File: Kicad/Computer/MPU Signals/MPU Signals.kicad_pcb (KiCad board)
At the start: 2 copper layers, 128.3 x 61 mm, 79 parts, among them IC1 FAN2558S38X, IC10 74LVC1G17GV,125, IC11 ATF22V10C-10SU, IC12 ATF22V10C-10SU, IC13 ATF22V10C-10SU, IC14 ATF22V10C-10SU, IC2 W65C816S6TQG-14, IC3 74LVC573AD,112, IC4 74LVC4245APW,118, IC5 74LVC04AD,118, IC6 74LVC32APW,118, IC7 74LVC1G08GV,125, IC8 74LVC11PW,112, IC9 NE555DRG4, J1 Conn_01x02_Male, J10 Conn_01x02_Male, J11 Conn_01x10_Male, J12 Conn_01x16_Male, J13 Conn_01x08_Male, J14 Conn_01x12_Male, J15 Conn_01x16_Male, J16 Conn_01x12_Male, J17 Conn_02x05_Counter_Clockwise, J18 Conn_02x05_Counter_Clockwise, J19 SamacSys_Parts:Pin_Header_1.2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, J2 Conn_01x02_Male, J20 Conn_02x05_Counter_Clockwise, J21 SamacSys_Parts:Pin_Header_1.2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, J22 Conn_02x05_Counter_Clockwise, J23 SamacSys_Parts:Pin_Header_1.2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, J24 Conn_02x05_Counter_Clockwise, J3 Conn_01x02_Male, J4 Conn_01x10_Male, J5 Conn_01x02_Male, J6 Conn_01x02_Male, J7 Conn_01x16_Male, J8 Conn_01x02_Male, J9 Conn_01x02_Male

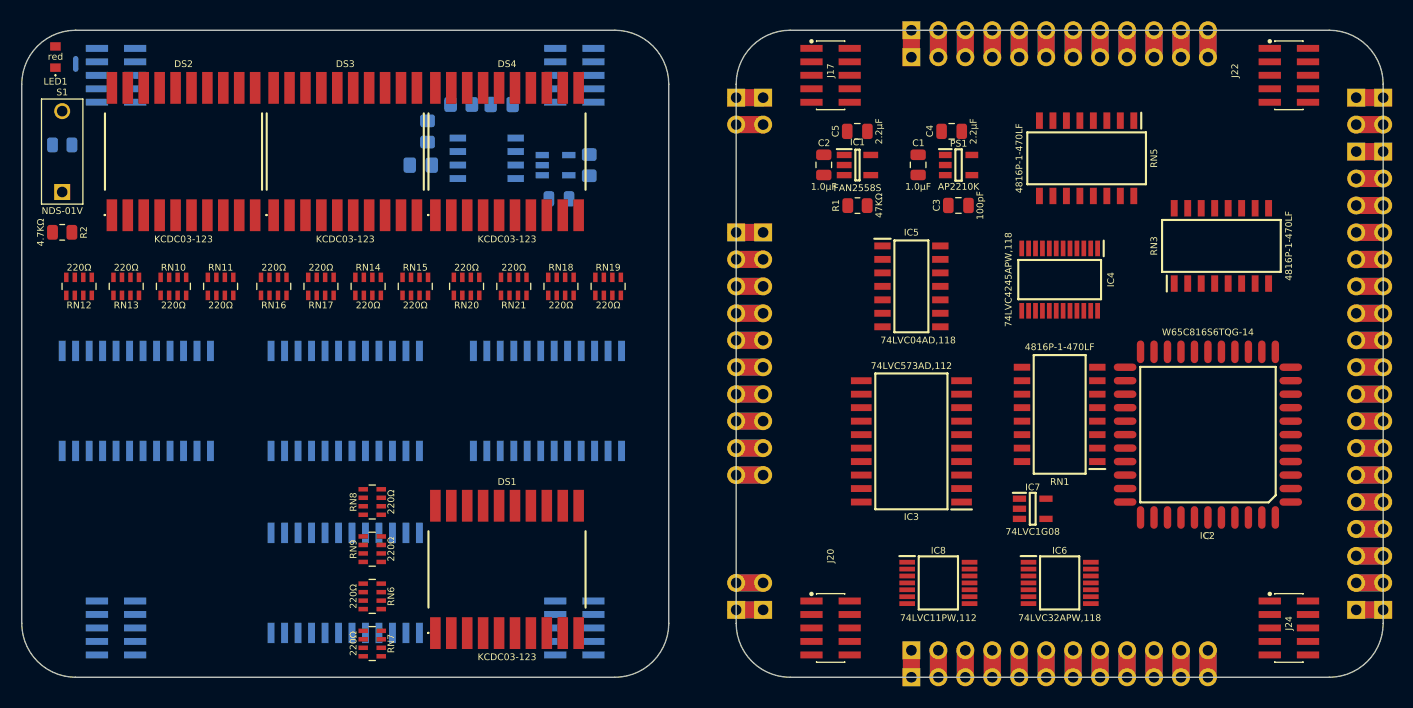
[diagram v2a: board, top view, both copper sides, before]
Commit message: Added a correct W65C816S footprint.
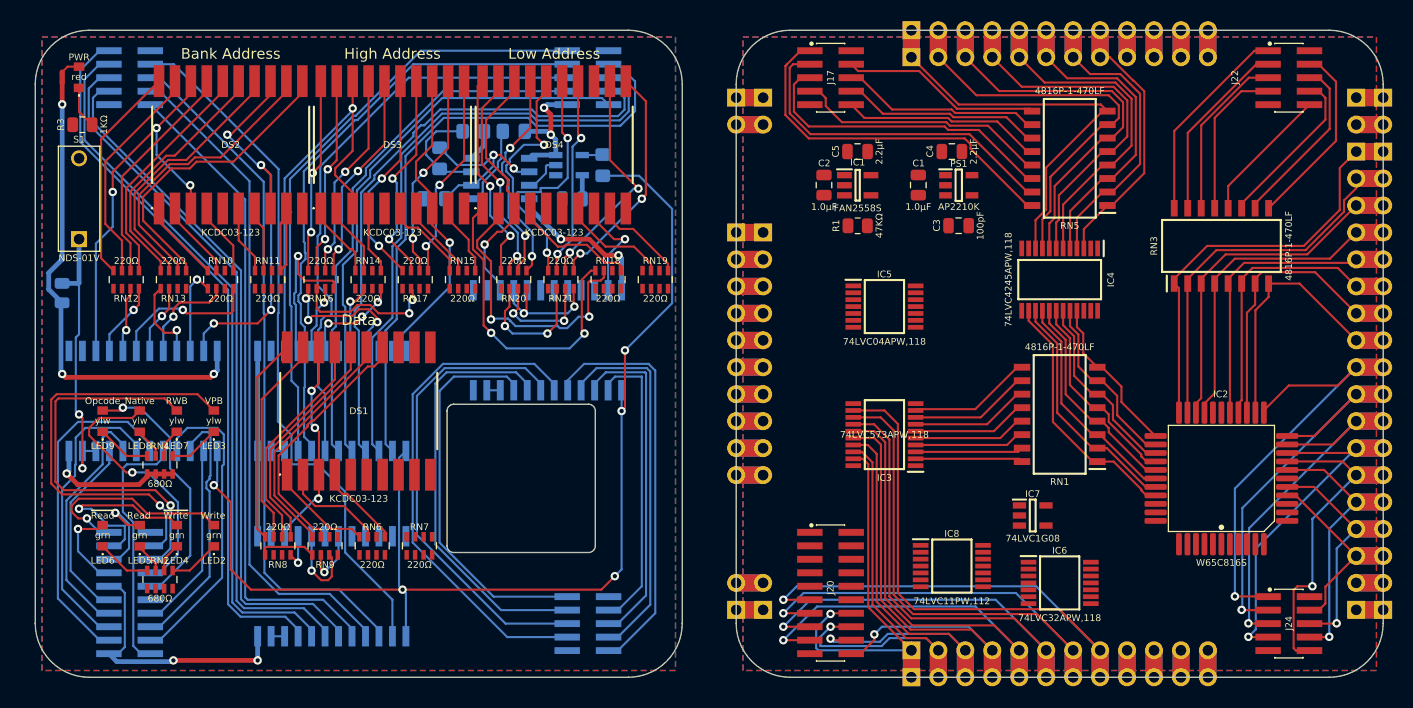
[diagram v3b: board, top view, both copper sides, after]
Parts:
- added LED2: 150224VS73100A, SamacSys_Parts:150224VS73100A, F.Cu at (77.8, 122.6)
- added LED3: 150224YS73100A, SamacSys_Parts:150224BS73100A, F.Cu at (77.8, 111.8)
- added LED4: 150224VS73100A, SamacSys_Parts:150224VS73100A, F.Cu at (74.3, 122.6)
- added LED5: 150224VS73100A, SamacSys_Parts:150224VS73100A, F.Cu at (70.8, 122.6)
- added LED6: 150224VS73100A, SamacSys_Parts:150224VS73100A, F.Cu at (67.3, 122.6)
- added LED7: 150224YS73100A, SamacSys_Parts:150224BS73100A, F.Cu at (74.3, 111.8)
- added LED8: 150224YS73100A, SamacSys_Parts:150224BS73100A, F.Cu at (70.8, 111.8)
- added LED9: 150224YS73100A, SamacSys_Parts:150224BS73100A, F.Cu at (67.3, 111.8)
- added RN2: CAY16-681J4LF, SamacSys_Parts:CAY16-J4, F.Cu at (72.7, 126.7)
- added RN4: CAY16-681J4LF, SamacSys_Parts:CAY16-J4, F.Cu at (72.7, 115.9)
- IC2: value W65C816S6TQG-14 -> W65C816S; footprint SamacSys_Parts:PLCC127P1752X1752X457-44N -> SamacSys_Parts:W65C816 PLCC 0.8mm 44 Pin
- IC3: value 74LVC573AD,112 -> 74LVC573APW,118; footprint SamacSys_Parts:SOIC127P1032X265-20N -> SamacSys_Parts:SOP65P640X110-20N
- IC5: value 74LVC04AD,118 -> 74LVC04APW,118; footprint SamacSys_Parts:SOIC127P600X175-14N -> SamacSys_Parts:SOP65P640X110-14N
- J19: footprint SamacSys_Parts:Pin_Header_1.27mm 2x05 -> SamacSys_Parts:Pin_Header_1.27mm 2x10
- J20: footprint SamacSys_Parts:Pin_Socket_1.27mm 2x05 -> SamacSys_Parts:Pin_Socket_1.27mm 2x10
- NT1, R3: moved to F.Cu
- R2: moved to B.Cu
- moved DS1 20.4 mm to (91.4, 110.8)
- moved RN7 10.2 mm to (97.2, 123.5), turned to 0 degrees
- moved RN8 9.80 mm to (83.8, 123.5), turned to 180 degrees
- moved RN17 8.91 mm to (96.8, 98.4)
- moved R2 5.72 mm to (63.5, 99.7), turned to 0 degrees
- moved IC14 5.72 mm to (109.2, 104.1)
- moved RN6 4.76 mm to (92.7, 123.5), turned to 0 degrees
- moved S1 4.72 mm to (65.1, 94.6)
- moved RN11 4.49 mm to (82.9, 98.4)
- moved RN13 4.49 mm to (74.0, 98.4)
- moved RN15 4.49 mm to (101.2, 98.4)
- moved DS2 4.49 mm to (79.4, 85.7)
- moved DS3 4.49 mm to (94.6, 85.7)
- moved DS4 4.49 mm to (109.9, 85.7)
- moved RN10 4.49 mm to (78.4, 98.4)
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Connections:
- IC4 pad 1: unconnected-(IC4-Pad1) -> /5V
- IC5 pad 11: unconnected-(IC5-Pad11) -> GND
- IC5 pad 13: unconnected-(IC5-Pad13) -> GND
- IC5 pad 9: unconnected-(IC5-Pad9) -> GND
- J15 pad 1: /BA7 -> /BA0
- J15 pad 2: /BA6 -> /BA1
- J15 pad 3: /BA5 -> /BA2
- J15 pad 4: /BA4 -> /BA3
- J15 pad 5: /BA3 -> /BA4
- J15 pad 6: /BA2 -> /BA5
- J15 pad 7: /BA1 -> /BA6
- J15 pad 8: /BA0 -> /BA7
- J16 pad 1: /BA7 -> /BA0
- J16 pad 2: /BA6 -> /BA1
- J16 pad 3: /BA5 -> /BA2
- J16 pad 4: /BA4 -> /BA3
- J16 pad 5: /BA3 -> /BA4
- J16 pad 6: /BA2 -> /BA5
- J16 pad 7: /BA1 -> /BA6
- J16 pad 8: /BA0 -> /BA7
- J19 pad 1: /5V_{TOP} -> /3.8V_{TOP}
- J19 pad 10: /BA7_{TOP} -> /BA3_{TOP}
- J19 pad 2: /BA0_{TOP} -> /~{VP}_{TOP}
- J19 pad 3: /BA1_{TOP} -> /R~{W}_{TOP}
- J19 pad 4: /BA2_{TOP} -> /Native Mode_{TOP}
- J19 pad 5: /BA3_{TOP} -> /Opcode Address_{TOP}
- J19 pad 6: /GND_{TOP} -> /5V_{TOP}
- J19 pad 7: /BA4_{TOP} -> /BA0_{TOP}
- J19 pad 8: /BA5_{TOP} -> /BA1_{TOP}
- J19 pad 9: /BA6_{TOP} -> /BA2_{TOP}
- J20 pad 1: /BA7 -> /~{VP}
- J20 pad 10: /5V -> GND
- J20 pad 2: /BA6 -> /R~{W}
- J20 pad 3: /BA5 -> /Native Mode
- J20 pad 4: /BA4 -> /Opcode Address
- J20 pad 6: /BA3 -> /BA7
- J20 pad 7: /BA2 -> /BA6
- J20 pad 8: /BA1 -> /BA5
- J20 pad 9: /BA0 -> /BA4
- J23 pad 6: unconnected-(J23-Pad6) -> /GND_{TOP}
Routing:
- net /Clock: track 0.00 -> 114.1 mm, vias 0 -> 5
- net /BA7: track 5.08 -> 82.4 mm, vias 0 -> 1
- net /BA6: track 5.08 -> 76.8 mm, vias 0 -> 1
- net /GND_{TOP}: track 0.00 -> 66.6 mm, vias 0 -> 5
- net /LD7_{TOP}: track 0.00 -> 66.3 mm
- net /LD0_{TOP}: track 0.00 -> 66.1 mm
- net /BA5: track 5.08 -> 71.0 mm, vias 0 -> 1
- net /LD6_{TOP}: track 0.00 -> 65.6 mm
- net /LD5_{TOP}: track 0.00 -> 65.6 mm
- net /LD4_{TOP}: track 0.00 -> 64.9 mm
- net /LD1_{TOP}: track 0.00 -> 64.4 mm
- net /5V_{TOP}: track 0.00 -> 62.8 mm, vias 0 -> 5
- net /LD3_{TOP}: track 0.00 -> 62.1 mm
- net /LD2_{TOP}: track 0.00 -> 61.6 mm
- net /BA4: track 5.08 -> 65.6 mm, vias 0 -> 1
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- added copper zone on B.Cu, net /GND_{TOP}
- added copper zone on F.Cu, net /GND_{TOP}
- added copper zone on B.Cu, net GND
- added copper zone on F.Cu, net GND
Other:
- board size 128.3 x 61 mm -> 127 x 61 mm
- board text added: "Bank Address"
- board text added: "Data"
- board text added: "High Address"
- board text added: "Low Address"
- board text added: "Native"
- board text added: "Opcode"
- board text added: "PWR"
- board text added: "RWB"
- board text added: "Read"
- board text added: "VPB"
- board text added: "Write"
- board text added: "~{Read}"
- board text added: "~{Write}"

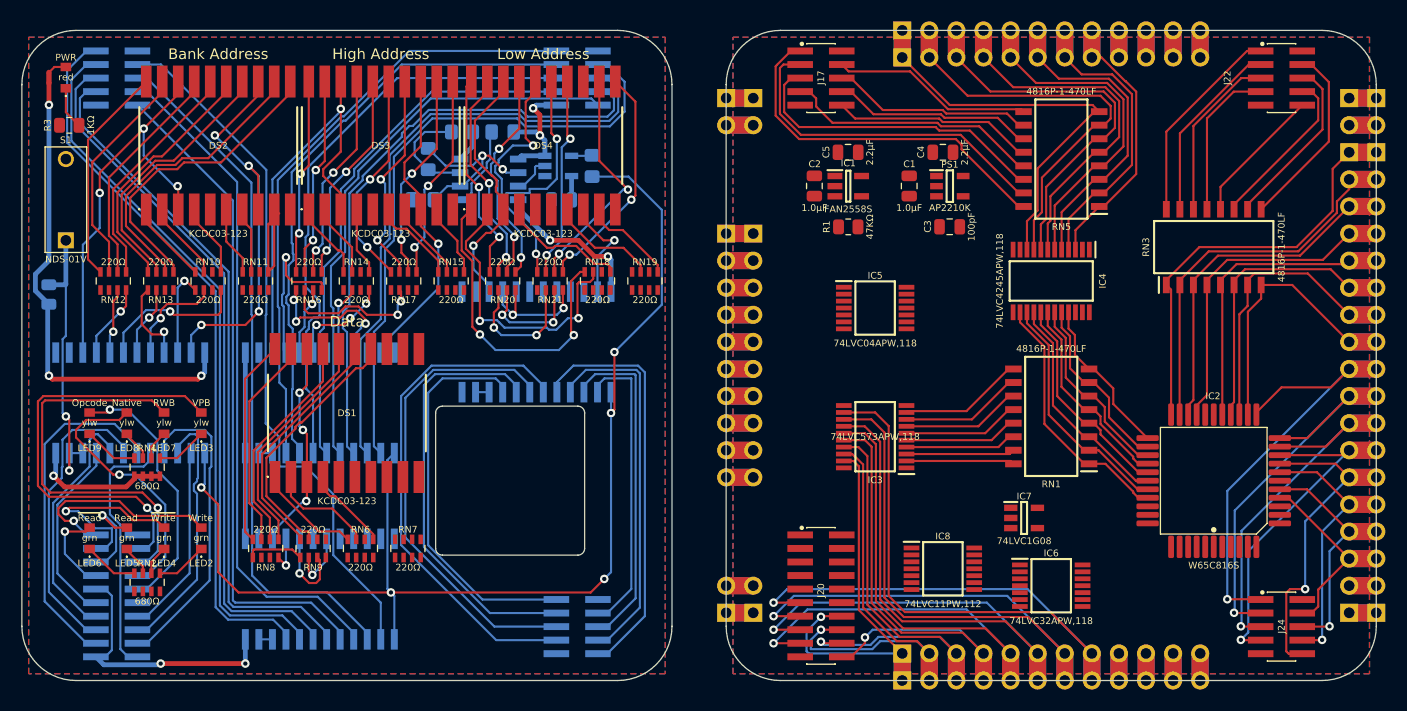
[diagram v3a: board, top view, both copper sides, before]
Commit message: Routed MPU board.
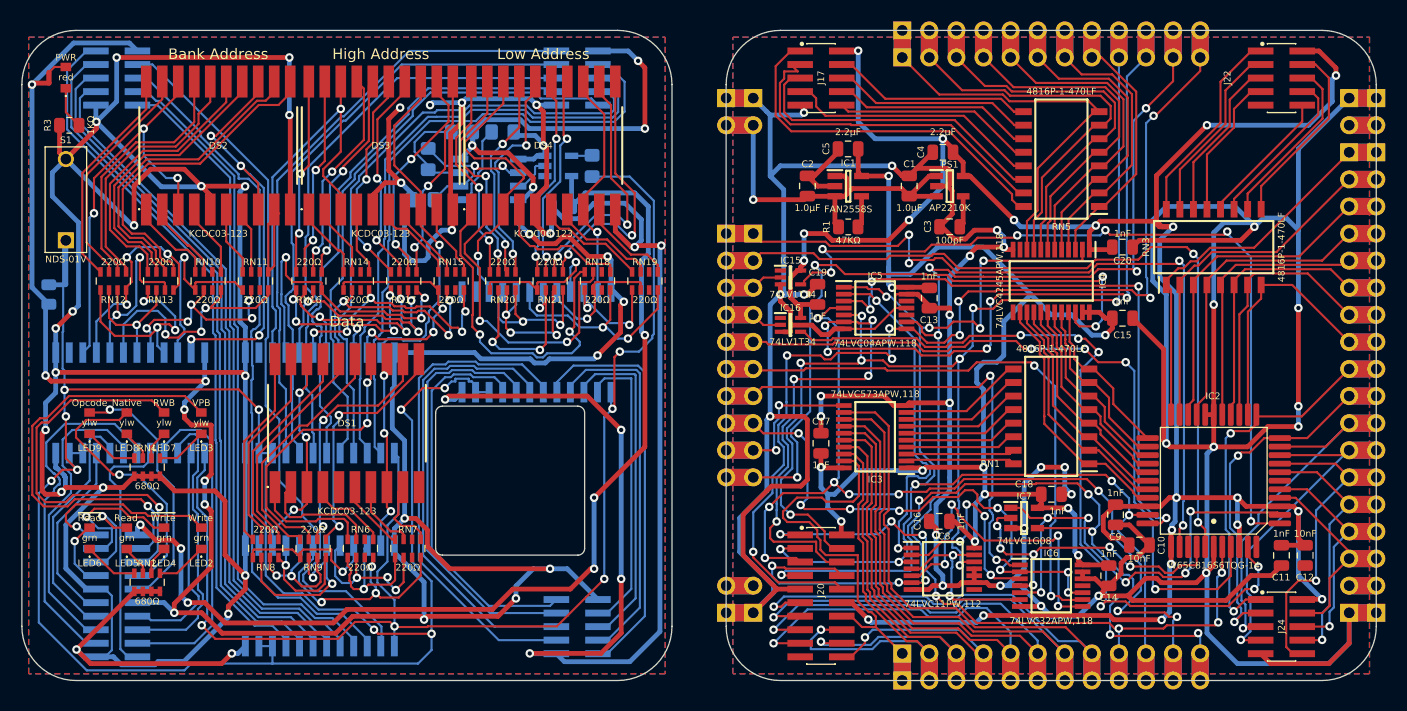
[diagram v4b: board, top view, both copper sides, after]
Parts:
- added C10: C_0805, SamacSys_Parts:C_0805, F.Cu at (165.7, 123.2)
- added C11: C_0805, SamacSys_Parts:C_0805, F.Cu at (179.1, 124.1)
- added C12: C_0805, SamacSys_Parts:C_0805, F.Cu at (181.3, 124.1)
- added C13: C_0805, SamacSys_Parts:C_0805, F.Cu at (146.1, 100.0)
- added C14: C_0805, SamacSys_Parts:C_0805, F.Cu at (162.9, 126.0)
- added C15: C_0805, SamacSys_Parts:C_0805, F.Cu at (164.1, 101.9)
- added C16: C_0805, SamacSys_Parts:C_0805, F.Cu at (147.0, 121.0)
- added C17: C_0805, SamacSys_Parts:C_0805, F.Cu at (135.9, 113.7)
- added C18: C_0805, SamacSys_Parts:C_0805, F.Cu at (157.5, 118.4)
- added C19: C_0805, SamacSys_Parts:C_0805, F.Cu at (135.6, 99.7)
- added C20: C_0805, SamacSys_Parts:C_0805, F.Cu at (164.1, 95.2)
- added C9: C_0805, SamacSys_Parts:C_0805, F.Cu at (163.5, 120.3)
- added IC15: 74LV1T34GWH, SamacSys_Parts:SOT65P212X110-5N, F.Cu at (133.0, 98.1)
- added IC16: 74LV1T34GWH, SamacSys_Parts:SOT65P212X110-5N, F.Cu at (133.0, 102.5)
- IC2: value W65C816S -> W65C816S6TQG-14
- moved DS1 0.95 mm to (91.4, 111.8)
- moved C2 0.65 mm to (134.6, 89.5)
- moved IC11 0.64 mm to (88.9, 128.0)
- moved C6 0.62 mm to (111.6, 91.4)
- moved C5 0.32 mm to (138.4, 86.0)
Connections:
- net /Read_Enable_{TOP} renamed /Read Enable_{TOP}
- net /Write_Enable_{TOP} renamed /Write Enable_{TOP}
- net /~{Read_Enable}_{TOP} renamed /~{Read Enable}_{TOP}
- net /~{Write_Enable}_{TOP} renamed /~{Write Enable}_{TOP}
- net 3V renamed /3.8V
- C1 pad 2: GND -> /GND
- C2 pad 2: GND -> /GND
- C3 pad 2: GND -> /GND
- C4 pad 2: GND -> /GND
- C5 pad 2: GND -> /GND
- IC1 pad 2: GND -> /GND
- IC2 pad 1: GND -> /GND
- IC2 pad 23: GND -> /GND
- IC2 pad 24: GND -> /GND
- IC2 pad 5: /~{IRQ} -> /~{IRQ}^{5V}
- IC2 pad 7: /~{NMI} -> /~{NMI}^{5V}
- IC3 pad 10: GND -> /GND
- IC4 pad 11: GND -> /GND
- IC4 pad 12: GND -> /GND
- IC4 pad 13: GND -> /GND
- IC5 pad 11: GND -> /GND
- IC5 pad 13: GND -> /GND
- IC5 pad 7: GND -> /GND
- IC5 pad 8: unconnected-(IC5-Pad8) -> /~{Read Enable}
- IC5 pad 9: GND -> /Read Enable
- IC6 pad 12: GND -> /GND
- IC6 pad 13: GND -> /GND
- IC6 pad 7: GND -> /GND
- IC7 pad 3: GND -> /GND
- IC8 pad 10: GND -> /GND
- IC8 pad 11: GND -> /GND
- IC8 pad 7: GND -> /GND
- IC8 pad 9: GND -> /GND
- J1 pad 1: GND -> /GND
- J10 pad 1: GND -> /GND
- J10 pad 2: unconnected-(J10-Pad2) -> Net-(J10-Pad2)
- J13 pad 10: /~{Write_Enable} -> /~{Write Enable}
- J13 pad 11: /Read_Enable -> /Read Enable
- J13 pad 12: /~{Read_Enable} -> /~{Read Enable}
- J13 pad 9: /Write_Enable -> /Write Enable
- J14 pad 10: /~{Write_Enable} -> /~{Write Enable}
- J14 pad 11: /Read_Enable -> /Read Enable
- J14 pad 12: /~{Read_Enable} -> /~{Read Enable}
- J14 pad 9: /Write_Enable -> /Write Enable
- J17 pad 5: GND -> /GND
- J2 pad 1: GND -> /GND
- J2 pad 2: unconnected-(J2-Pad2) -> Net-(J2-Pad2)
- J20 pad 10: GND -> /GND
- J20 pad 16: /~{Read_Enable} -> /~{Read Enable}
- J20 pad 17: /Read_Enable -> /Read Enable
- J20 pad 18: /~{Write_Enable} -> /~{Write Enable}
- J20 pad 19: /Write_Enable -> /Write Enable
- J20 pad 5: GND -> /GND
- J22 pad 5: GND -> /GND
- J24 pad 5: GND -> /GND
- J3 pad 1: GND -> /GND
- J5 pad 1: GND -> /GND
- J5 pad 2: unconnected-(J2-Pad2) -> Net-(J2-Pad2)
- J6 pad 1: GND -> /GND
- J6 pad 2: unconnected-(J6-Pad2) -> Net-(J6-Pad2)
- J8 pad 1: GND -> /GND
- J8 pad 2: unconnected-(J10-Pad2) -> Net-(J10-Pad2)
- J9 pad 1: GND -> /GND
- J9 pad 2: unconnected-(J6-Pad2) -> Net-(J6-Pad2)
- PS1 pad 2: GND -> /GND
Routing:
- net /GND: track 0.00 -> 503.0 mm, vias 0 -> 29
- net /GND_{TOP}: track 66.6 -> 464.5 mm, vias 5 -> 32
- net /5V: track 0.00 -> 225.0 mm, vias 0 -> 20
- net /5V_{TOP}: track 62.8 -> 262.6 mm, vias 5 -> 19
- net /~{LED Enable}: track 34.4 -> 176.5 mm, vias 2 -> 9
- net /3.8V: track 0.00 -> 126.4 mm, vias 0 -> 11
- net /Write Enable: track 0.00 -> 112.1 mm, vias 0 -> 8
- net /R~{W}: track 5.08 -> 115.3 mm, vias 0 -> 9
- net /~{Write Enable}: track 0.00 -> 106.2 mm, vias 0 -> 9
- net /Read Enable: track 0.00 -> 104.7 mm, vias 0 -> 7
- net /~{Read Enable}: track 0.00 -> 102.4 mm, vias 0 -> 8
- net /3.8V_{TOP}: track 2.20 -> 99.5 mm, vias 0 -> 6
- net /Native Mode: track 5.08 -> 90.0 mm, vias 0 -> 9
- net /~{NMI}^{5V}: track 0.00 -> 75.8 mm, vias 0 -> 6
- net /~{IRQ}^{5V}: track 0.00 -> 74.3 mm, vias 0 -> 6
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- added copper zone on B.Cu, net /GND
- added copper zone on F.Cu, net /GND
- removed copper zone on B.Cu, net GND
- removed copper zone on F.Cu, net GND

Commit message: Optimise address decoding when in MPU Lock.
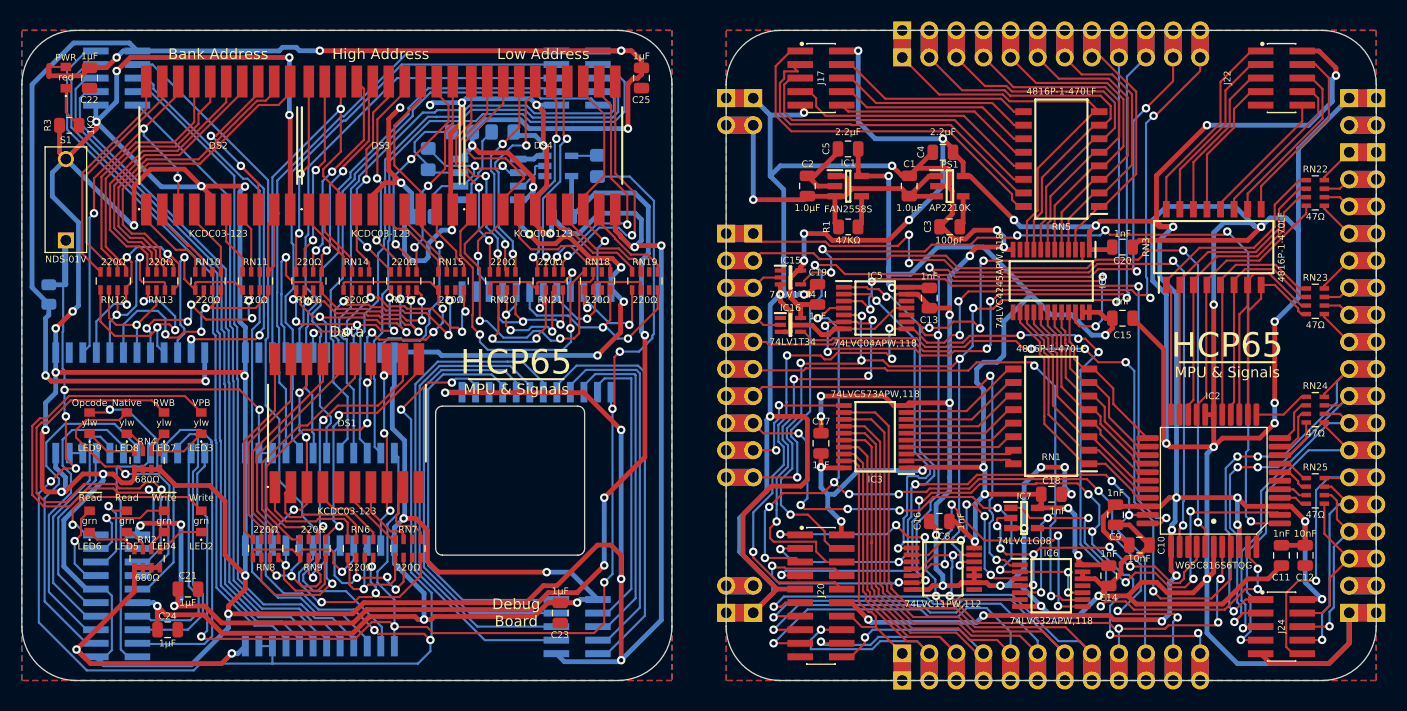
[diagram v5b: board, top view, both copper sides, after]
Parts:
- added C21: C_0805, SamacSys_Parts:C_0805, F.Cu at (76.5, 127.3)
- added C22: C_0805, SamacSys_Parts:C_0805, F.Cu at (67.3, 79.4)
- added C23: C_0805, SamacSys_Parts:C_0805, F.Cu at (111.4, 129.5)
- added C24: C_0805, SamacSys_Parts:C_0805, F.Cu at (74.6, 131.1)
- added C25: C_0805, SamacSys_Parts:C_0805, F.Cu at (119.1, 79.4)
- added RN22: CAY16-470J4LF, SamacSys_Parts:CAY16470J4LF, F.Cu at (182.2, 90.2)
- added RN23: CAY16-470J4LF, SamacSys_Parts:CAY16470J4LF, F.Cu at (182.2, 100.3)
- added RN24: CAY16-470J4LF, SamacSys_Parts:CAY16470J4LF, F.Cu at (182.2, 110.5)
- added RN25: CAY16-470J4LF, SamacSys_Parts:CAY16470J4LF, F.Cu at (182.2, 118.1)
- IC2: value W65C816S6TQG-14 -> W65C816S6TQG
- moved RN2 2.22 mm to (72.7, 124.5)
- moved LED2 1.59 mm to (77.8, 121.0)
- moved LED4 1.59 mm to (74.3, 121.0)
- moved LED5 1.59 mm to (70.8, 121.0)
- moved LED6 1.59 mm to (67.3, 121.0)
- moved C7 1.59 mm to (98.6, 92.4)
- moved C6 0.95 mm to (111.6, 92.4)
- moved NT1 0.64 mm to (63.5, 78.7)
- moved RN4 0.64 mm to (72.7, 115.3)
- moved R4 0.51 mm to (114.9, 87.6)
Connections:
- IC2 pad 10: /A0 -> Net-(IC2-Pad10)
- IC2 pad 11: /A1 -> Net-(IC2-Pad11)
- IC2 pad 13: /A2 -> Net-(IC2-Pad13)
- IC2 pad 14: /A3 -> Net-(IC2-Pad14)
- IC2 pad 15: /A4 -> Net-(IC2-Pad15)
- IC2 pad 16: /A5 -> Net-(IC2-Pad16)
- IC2 pad 17: /A6 -> Net-(IC2-Pad17)
- IC2 pad 18: /A7 -> Net-(IC2-Pad18)
- IC2 pad 19: /A8 -> Net-(IC2-Pad19)
- IC2 pad 20: /A9 -> Net-(IC2-Pad20)
- IC2 pad 21: /A10 -> Net-(IC2-Pad21)
- IC2 pad 22: /A11 -> Net-(IC2-Pad22)
- IC2 pad 25: /A12 -> Net-(IC2-Pad25)
- IC2 pad 26: /A13 -> Net-(IC2-Pad26)
- IC2 pad 27: /A14 -> Net-(IC2-Pad27)
- IC2 pad 28: /A15 -> Net-(IC2-Pad28)
- RN3 pad 1: /A15 -> Net-(IC2-Pad28)
- RN3 pad 2: /A14 -> Net-(IC2-Pad27)
- RN3 pad 3: /A13 -> Net-(IC2-Pad26)
- RN3 pad 4: /A12 -> Net-(IC2-Pad25)
- RN3 pad 5: /A11 -> Net-(IC2-Pad22)
- RN3 pad 6: /A10 -> Net-(IC2-Pad21)
- RN3 pad 7: /A9 -> Net-(IC2-Pad20)
- RN3 pad 8: /A8 -> Net-(IC2-Pad19)
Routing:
- net /GND_{TOP}: track 464.5 -> 500.3 mm
- net /5V_{TOP}: track 262.6 -> 294.5 mm, vias 19 -> 17
- net /A15: track 40.1 -> 8.65 mm
- net Net-(IC2-Pad28): track 0.00 -> 31.0 mm
- net /A14: track 37.5 -> 7.77 mm
- net Net-(IC2-Pad27): track 0.00 -> 29.2 mm
- net /A13: track 34.0 -> 7.77 mm
- net Net-(IC2-Pad26): track 0.00 -> 26.2 mm
- net Net-(IC2-Pad25): track 0.00 -> 24.2 mm
- net /A12: track 31.8 -> 8.65 mm
- net Net-(IC2-Pad22): track 0.00 -> 22.1 mm
- net /A9: track 29.5 -> 7.77 mm
- net /A11: track 29.9 -> 8.65 mm
- net /A10: track 28.4 -> 7.77 mm
- net /A8: track 28.8 -> 8.65 mm
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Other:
- board text added: "Debug Board"
- board text added: "HCP65"
- board text added: "MPU & Signals"
